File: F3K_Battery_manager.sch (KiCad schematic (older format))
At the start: 14 parts

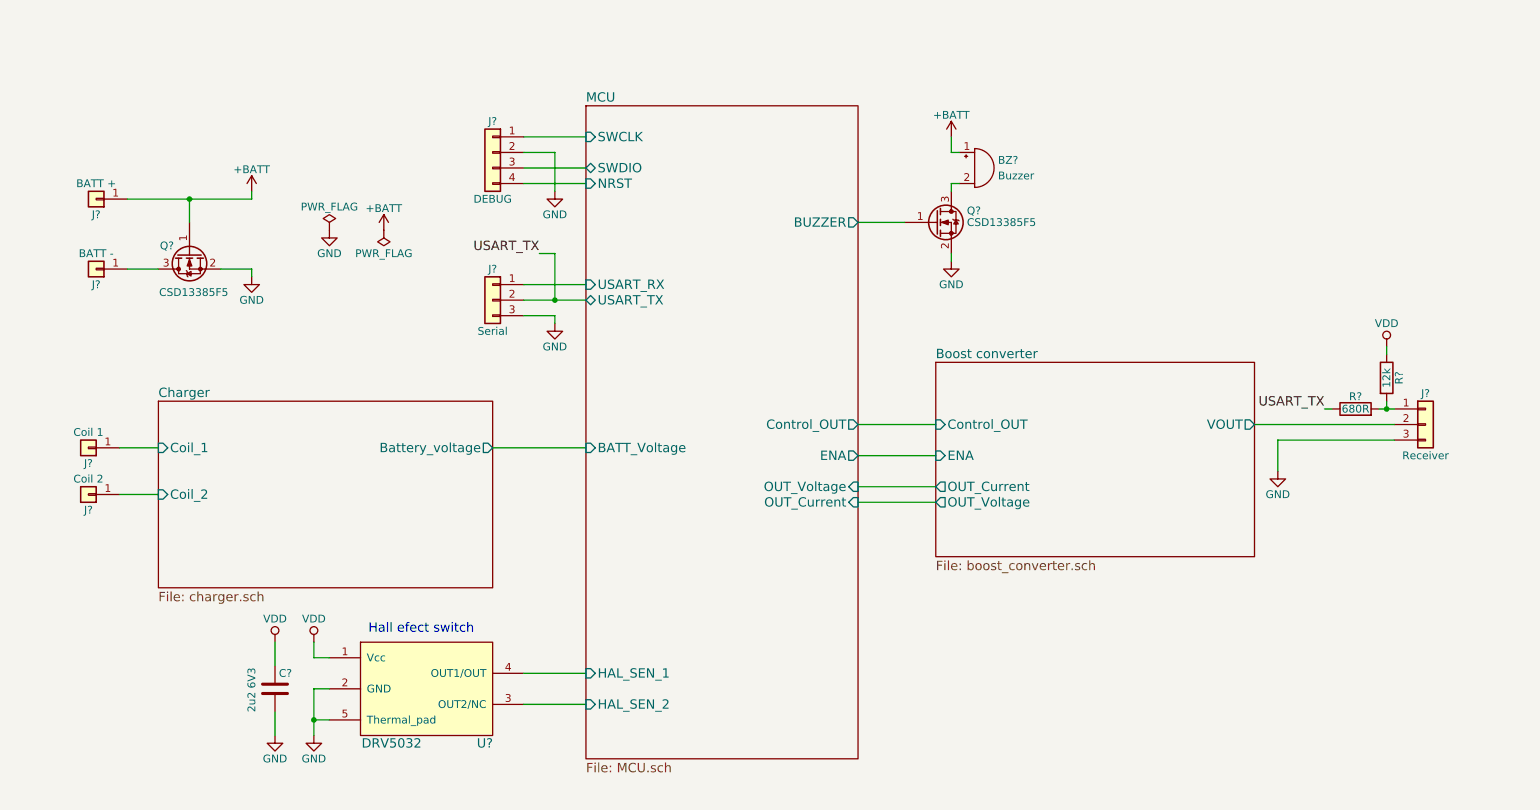
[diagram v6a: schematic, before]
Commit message: added few MPNs
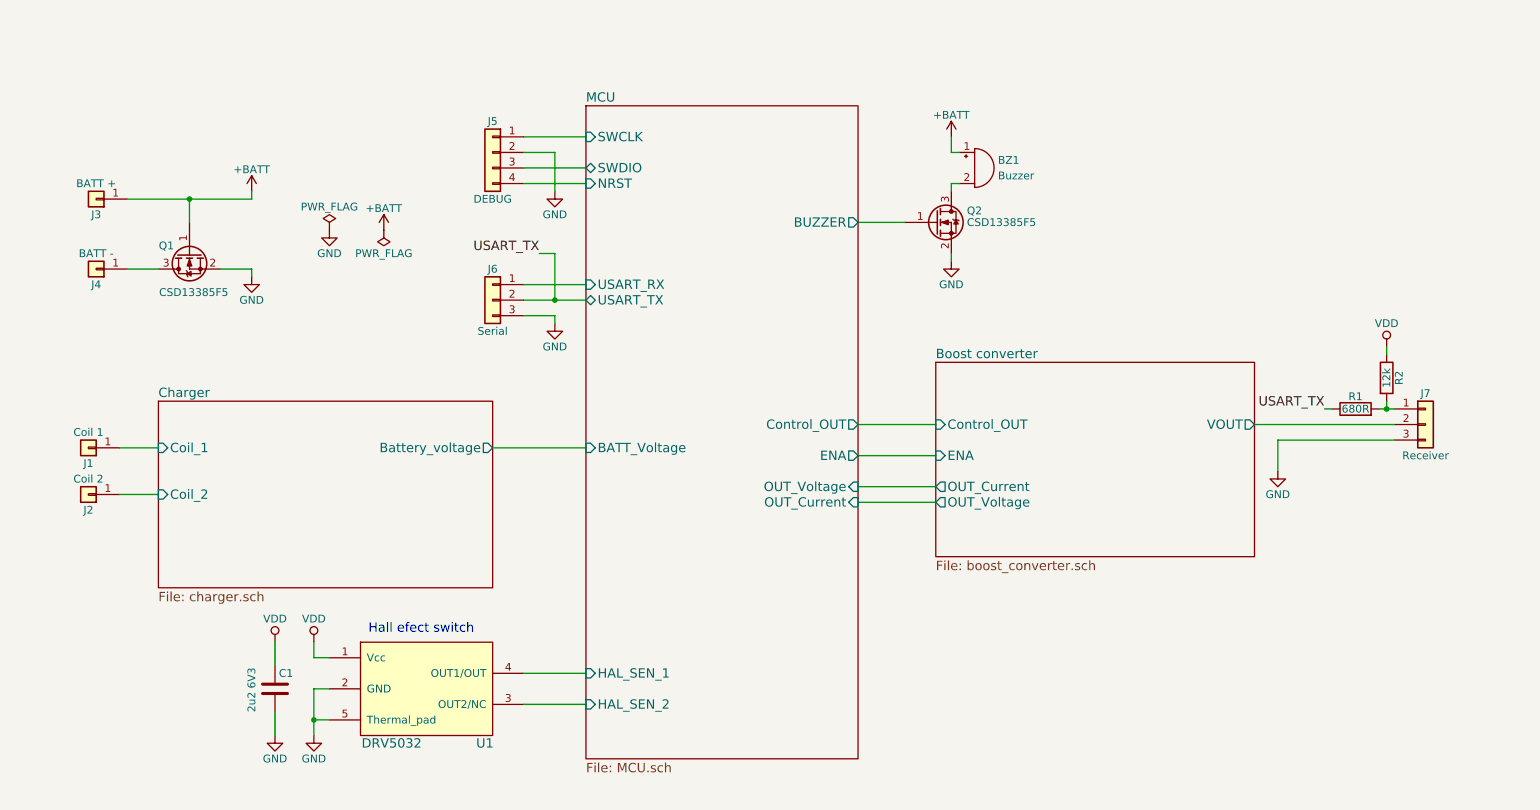
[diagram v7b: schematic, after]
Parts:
- C1: renamed from C?; footprint (none) -> Capacitors_SMD:C_0402; MPN (none) -> GRM155D80J225KE95D
- gave numbers to parts that had none: 13
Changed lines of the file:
@@
 $EndSheet
 $Comp
-L Conn_01x04 J?
+L Conn_01x04 J5
 U 1 1 5AA070CB
 P 4250 2250
-F 0 "J?" H 4250 2450 50  0000 C CNN
+F 0 "J5" H 4250 2450 50  0000 C CNN
 F 1 "DEBUG" H 4250 1950 50  0000 C CNN
 F 2 "" H 4250 2250 50  0001 C CNN
@@
 $EndComp
 $Comp
-L GND #PWR?
+L GND #PWR9
 U 1 1 5AA0735F
 P 4650 2500
-F 0 "#PWR?" H 4650 2250 50  0001 C CNN
+F 0 "#PWR9" H 4650 2250 50  0001 C CNN
 F 1 "GND" H 4650 2350 50  0000 C CNN
 F 2 "" H 4650 2500 50  0001 C CNN
@@
 $EndComp
 $Comp
-L GND #PWR?
+L GND #PWR10
 U 1 1 5AA07C91
 P 4650 3350
-F 0 "#PWR?" H 4650 3100 50  0001 C CNN
+F 0 "#PWR10" H 4650 3100 50  0001 C CNN
 F 1 "GND" H 4650 3200 50  0000 C CNN
 F 2 "" H 4650 3350 50  0001 C CNN
@@
 $EndComp
 $Comp
-L DRV5032 U?
+L DRV5032 U1
 U 1 1 5AA08B55
 P 3850 5700
-F 0 "U?" H 4200 5350 60  0000 C CNN
+F 0 "U1" H 4200 5350 60  0000 C CNN
 F 1 "DRV5032" H 3600 5350 60  0000 C CNN
 F 2 "lakotamm-sensor:X2SON_4_1.10x1.40mm" H 3900 5250 60  0001 C CNN
@@
 $EndComp
 $Comp
-L C C?
+L C C1
 U 1 1 5AA08E27
 P 2850 5700
-F 0 "C?" H 2875 5800 50  0000 L CNN
+F 0 "C1" H 2875 5800 50  0000 L CNN
 F 1 "2u2 6V3" V 2700 5550 50  0000 L CNN
-F 2 "" H 2888 5550 50  0001 C CNN
+F 2 "Capacitors_SMD:C_0402" H 2888 5550 50  0001 C CNN
 F 3 "" H 2850 5700 50  0001 C CNN
+F 4 "GRM155D80J225KE95D" H 2850 5700 60  0001 C CNN "MPN"
 	1    2850 5700
 	1    0    0    -1
@@
 	4850 3100 4450 3100
 Wire Wire Line
-	4450 3200 4650 3200
-Wire Wire Line
-	4650 3200 4850 3200
+	4450 3200 4850 3200
 Wire Wire Line
 	4450 3300 4650 3300
@@
 	4650 3300 4650 3350
 $Comp
-L GND #PWR?
+L GND #PWR6
 U 1 1 5AA09559
 P 3100 6000
-F 0 "#PWR?" H 3100 5750 50  0001 C CNN
+F 0 "#PWR6" H 3100 5750 50  0001 C CNN
 F 1 "GND" H 3100 5850 50  0000 C CNN
 F 2 "" H 3100 6000 50  0001 C CNN
@@
 	3200 5700 3100 5700
 Wire Wire Line
-	3100 5700 3100 5900
-Wire Wire Line
-	3100 5900 3100 6000
+	3100 5700 3100 6000
 Wire Wire Line
 	3200 5900 3100 5900
 Connection ~ 3100 5900
 $Comp
-L VDD #PWR?
+L VDD #PWR5
 U 1 1 5AA0982A
 P 3100 5400
-F 0 "#PWR?" H 3100 5250 50  0001 C CNN
+F 0 "#PWR5" H 3100 5250 50  0001 C CNN
 F 1 "VDD" H 3100 5550 50  0000 C CNN
 F 2 "" H 3100 5400 50  0001 C CNN
@@
 	3100 5500 3200 5500
 $Comp
-L VDD #PWR?
+L VDD #PWR3
 U 1 1 5AA09936
 P 2850 5400
-F 0 "#PWR?" H 2850 5250 50  0001 C CNN
+F 0 "#PWR3" H 2850 5250 50  0001 C CNN
 F 1 "VDD" H 2850 5550 50  0000 C CNN
 F 2 "" H 2850 5400 50  0001 C CNN
@@
 $EndComp
 $Comp
-L GND #PWR?
+L GND #PWR4
 U 1 1 5AA0996B
 P 2850 6000
-F 0 "#PWR?" H 2850 5750 50  0001 C CNN
+F 0 "#PWR4" H 2850 5750 50  0001 C CNN
 F 1 "GND" H 2850 5850 50  0000 C CNN
 F 2 "" H 2850 6000 50  0001 C CNN
@@
 	4450 5800 4850 5800
 $Comp
-L PWR_FLAG #FLG?
+L PWR_FLAG #FLG1
 U 1 1 5AA0B07D
 P 3200 2750
-F 0 "#FLG?" H 3200 2825 50  0001 C CNN
+F 0 "#FLG1" H 3200 2825 50  0001 C CNN
 F 1 "PWR_FLAG" H 3200 2900 50  0000 C CNN
 F 2 "" H 3200 2750 50  0001 C CNN
@@
 $EndComp
 $Comp
-L GND #PWR?
+L GND #PWR7
 U 1 1 5AA0B18B
 P 3200 2750
-F 0 "#PWR?" H 3200 2500 50  0001 C CNN
+F 0 "#PWR7" H 3200 2500 50  0001 C CNN
 F 1 "GND" H 3200 2600 50  0000 C CNN
 F 2 "" H 3200 2750 50  0001 C CNN
@@
 $EndComp
 $Comp
-L PWR_FLAG #FLG?
+L PWR_FLAG #FLG2
 U 1 1 5AA0B25E
 P 3550 2750
-F 0 "#FLG?" H 3550 2825 50  0001 C CNN
+F 0 "#FLG2" H 3550 2825 50  0001 C CNN
 F 1 "PWR_FLAG" H 3550 2900 50  0000 C CNN
 F 2 "" H 3550 2750 50  0001 C CNN
@@
 $EndComp
 $Comp
-L +BATT #PWR?
+L +BATT #PWR8
 U 1 1 5AA0B29D
 P 3550 2750
-F 0 "#PWR?" H 3550 2600 50  0001 C CNN
+F 0 "#PWR8" H 3550 2600 50  0001 C CNN
 F 1 "+BATT" H 3550 2890 50  0000 C CNN
 F 2 "" H 3550 2750 50  0001 C CNN
@@
 $EndComp
 $Comp
-L Buzzer BZ?
+L Buzzer BZ1
 U 1 1 5AA0FFE4
 P 7350 2350
-F 0 "BZ?" H 7500 2400 50  0000 L CNN
+F 0 "BZ1" H 7500 2400 50  0000 L CNN
 F 1 "Buzzer" H 7500 2300 50  0000 L CNN
 F 2 "" V 7325 2450 50  0001 C CNN
@@
 	7200 2450 7200 2500
 $Comp
-L GND #PWR?
+L GND #PWR12
 U 1 1 5AA112B0
 P 7200 2950
-F 0 "#PWR?" H 7200 2700 50  0001 C CNN
+F 0 "#PWR12" H 7200 2700 50  0001 C CNN
 F 1 "GND" H 7200 2800 50  0000 C CNN
 F 2 "" H 7200 2950 50  0001 C CNN
@@
 $EndSheet
 $Comp
-L +BATT #PWR?
+L +BATT #PWR11
 U 1 1 5AA3F1DA
 P 7200 2150
-F 0 "#PWR?" H 7200 2000 50  0001 C CNN
+F 0 "#PWR11" H 7200 2000 50  0001 C CNN
 F 1 "+BATT" H 7200 2290 50  0000 C CNN
 F 2 "" H 7200 2150 50  0001 C CNN
@@
 	6600 4000 7100 4000
 $Comp
-L Conn_01x03 J?
+L Conn_01x03 J7
 U 1 1 5AA45C5D
 P 10250 4000
-F 0 "J?" H 10250 4200 50  0000 C CNN
+F 0 "J7" H 10250 4200 50  0000 C CNN
 F 1 "Receiver" H 10250 3800 50  0000 C CNN
 F 2 "" H 10250 4000 50  0001 C CNN
@@
 	9150 4000 10050 4000
 $Comp
-L GND #PWR?
+L GND #PWR13
 U 1 1 5AA460B2
 P 9300 4300
-F 0 "#PWR?" H 9300 4050 50  0001 C CNN
+F 0 "#PWR13" H 9300 4050 50  0001 C CNN
 F 1 "GND" H 9300 4150 50  0000 C CNN
 F 2 "" H 9300 4300 50  0001 C CNN
@@
 	9300 4100 9300 4300
 $Comp
-L Conn_01x03 J?
+L Conn_01x03 J6
 U 1 1 5AA46769
 P 4250 3200
-F 0 "J?" H 4250 3400 50  0000 C CNN
+F 0 "J6" H 4250 3400 50  0000 C CNN
 F 1 "Serial" H 4250 3000 50  0000 C CNN
 F 2 "" H 4250 3200 50  0001 C CNN
@@
 Hall efect switch\n
 $Comp
-L R R?
+L R R1
 U 1 1 5AA59CAF
 P 9800 3900
-F 0 "R?" V 9880 3900 50  0000 C CNN
+F 0 "R1" V 9880 3900 50  0000 C CNN
 F 1 "680R" V 9800 3900 50  0000 C CNN
 F 2 "" V 9730 3900 50  0001 C CNN
@@
 $EndComp
 Wire Wire Line
-	9950 3900 10000 3900
-Wire Wire Line
-	10000 3900 10050 3900
+	9950 3900 10050 3900
 Text Label 4550 2900 2    60   ~ 0
 USART_TX
@@
 	9600 3900 9650 3900
 $Comp
-L R R?
+L R R2
 U 1 1 5AA65085
 P 10000 3700
-F 0 "R?" V 10080 3700 50  0000 C CNN
+F 0 "R2" V 10080 3700 50  0000 C CNN
 F 1 "12k" V 10000 3700 50  0000 C CNN
 F 2 "" V 9930 3700 50  0001 C CNN
@@
 Connection ~ 10000 3900
 $Comp
-L VDD #PWR?
+L VDD #PWR14
 U 1 1 5AA65702
 P 10000 3500
-F 0 "#PWR?" H 10000 3350 50  0001 C CNN
+F 0 "#PWR14" H 10000 3350 50  0001 C CNN
 F 1 "VDD" H 10000 3650 50  0000 C CNN
 F 2 "" H 10000 3500 50  0001 C CNN
@@
 	4250 4150 4850 4150
 $Comp
-L CSD13385F5 Q?
+L CSD13385F5 Q2
 U 1 1 5AA727C4
 P 7100 2700
-F 0 "Q?" H 7300 2775 50  0000 L CNN
+F 0 "Q2" H 7300 2775 50  0000 L CNN
 F 1 "CSD13385F5" H 7300 2700 50  0000 L CNN
 F 2 "" H 7300 2625 50  0001 L CIN
@@
 $EndComp
 $Comp
-L CSD13385F5 Q?
+L CSD13385F5 Q1
 U 1 1 5AA728A9
 P 2300 2900
-F 0 "Q?" V 2250 3000 50  0000 L CNN
+F 0 "Q1" V 2250 3000 50  0000 L CNN
 F 1 "CSD13385F5" V 2550 2650 50  0000 L CNN
 F 2 "" H 2500 2825 50  0001 L CIN
@@
 $EndComp
 $Comp
-L Conn_01x01 J?
+L Conn_01x01 J3
 U 1 1 5AA73103
 P 1700 2550
-F 0 "J?" H 1700 2650 50  0000 C CNN
+F 0 "J3" H 1700 2650 50  0000 C CNN
 F 1 "BATT +" H 1700 2450 50  0000 C CNN
 F 2 "" H 1700 2550 50  0001 C CNN
@@
 $EndComp
 $Comp
-L Conn_01x01 J?
+L Conn_01x01 J4
 U 1 1 5AA7332B
 P 1700 3000
-F 0 "J?" H 1700 3100 50  0000 C CNN
+F 0 "J4" H 1700 3100 50  0000 C CNN
 F 1 "BATT -" H 1700 2900 50  0000 C CNN
 F 2 "" H 1700 3000 50  0001 C CNN
@@
 	1900 3000 2100 3000
 Wire Wire Line
-	1900 2550 2300 2550
-Wire Wire Line
-	2300 2550 2700 2550
+	1900 2550 2700 2550
 Wire Wire Line
 	2300 2550 2300 2700
 $Comp
-L +BATT #PWR?
+L +BATT #PWR1
 U 1 1 5AA74E47
 P 2700 2500
-F 0 "#PWR?" H 2700 2350 50  0001 C CNN
+F 0 "#PWR1" H 2700 2350 50  0001 C CNN
 F 1 "+BATT" H 2700 2640 50  0000 C CNN
 F 2 "" H 2700 2500 50  0001 C CNN
@@
 Connection ~ 2300 2550
 $Comp
-L GND #PWR?
+L GND #PWR2
 U 1 1 5AA7526D
 P 2700 3050
-F 0 "#PWR?" H 2700 2800 50  0001 C CNN
+F 0 "#PWR2" H 2700 2800 50  0001 C CNN
 F 1 "GND" H 2700 2900 50  0000 C CNN
 F 2 "" H 2700 3050 50  0001 C CNN
@@
 	2700 3000 2700 3050
 $Comp
-L Conn_01x01 J?
+L Conn_01x01 J1
 U 1 1 5AA76BD4
 P 1650 4150
-F 0 "J?" H 1650 4250 50  0000 C CNN
+F 0 "J1" H 1650 4250 50  0000 C CNN
 F 1 "Coil 1" H 1650 4050 50  0000 C CNN
 F 2 "" H 1650 4150 50  0001 C CNN
@@
 $EndComp
 $Comp
-L Conn_01x01 J?
+L Conn_01x01 J2
 U 1 1 5AA76CB0
 P 1650 4450
-F 0 "J?" H 1650 4550 50  0000 C CNN
+F 0 "J2" H 1650 4550 50  0000 C CNN
 F 1 "Coil 2" H 1650 4350 50  0000 C CNN
 F 2 "" H 1650 4450 50  0001 C CNN

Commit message: Progress on the charging circuit
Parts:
- removed J1: Coil 1, symbol Conn_01x01
- removed J2: Coil 2, symbol Conn_01x01
- removed J3: BATT +, symbol Conn_01x01
- removed J4: BATT -, symbol Conn_01x01
- added J?: Battery, symbol Conn_01x04
- added J?: Coil, symbol Conn_01x02
- J5: value DEBUG -> Debug
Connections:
- net +BATT: now also J?.3 (Pin_3)
- net Charger/Coil_1: now also J?.2 (Pin_2)
- net Charger/Coil_2: now also J?.1 (Pin_1)
- net at Q1.3 (D): now also J?.4 (Pin_4)
- new net Thermistor: J?.2 (Pin_2)
- new net Thermistor_OFF: J?.1 (Pin_1)
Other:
- moved on the sheet: Q1
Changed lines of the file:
@@
 F7 "HAL_SEN_2" I L 4850 5800 60
 F8 "BUZZER" O R 6600 2700 60
-F9 "Control_OUT" O R 6600 4000 60
-F10 "ENA" O R 6600 4200 60
-F11 "OUT_Voltage" I R 6600 4400 60
-F12 "OUT_Current" I R 6600 4500 60
-F13 "BATT_Voltage" I L 4850 4150 60
-F14 "USART_TX" B L 4850 3200 60
+F9 "OUT_Voltage" I R 6600 4400 60
+F10 "OUT_Current" I R 6600 4500 60
+F11 "BATT_Voltage" I L 4850 4150 60
+F12 "USART_TX" B L 4850 3200 60
+F13 "~CHARGING" I L 4850 4350 60
+F14 "Voltage_control" O R 6600 4000 60
+F15 "Enable_boost" O R 6600 4200 60
 $EndSheet
 $Comp
@@
 P 4250 2250
 F 0 "J5" H 4250 2450 50  0000 C CNN
-F 1 "DEBUG" H 4250 1950 50  0000 C CNN
+F 1 "Debug" H 4250 1950 50  0000 C CNN
 F 2 "" H 4250 2250 50  0001 C CNN
 F 3 "" H 4250 2250 50  0001 C CNN
@@
 Wire Wire Line
 	6600 2700 6900 2700
-$Sheet
-S 2100 3850 2150 1200
-U 5AA3AC9F
-F0 "Charger" 60
-F1 "charger.sch" 60
-F2 "Coil_1" I L 2100 4150 60
-F3 "Coil_2" I L 2100 4450 60
-F4 "Battery_voltage" O R 4250 4150 60
-$EndSheet
 $Comp
 L +BATT #PWR11
@@
 F1 "boost_converter.sch" 60
 F2 "VOUT" O R 9150 4000 60
-F3 "Control_OUT" I L 7100 4000 60
-F4 "ENA" I L 7100 4200 60
-F5 "OUT_Current" O L 7100 4400 60
-F6 "OUT_Voltage" O L 7100 4500 60
+F3 "ENA" I L 7100 4200 60
+F4 "OUT_Current" O L 7100 4400 60
+F5 "OUT_Voltage" O L 7100 4500 60
+F6 "Voltage_control" I L 7100 4000 60
 $EndSheet
 Wire Wire Line
@@
 	10000 3500 10000 3550
 Wire Wire Line
-	1850 4150 2100 4150
-Wire Wire Line
 	4250 4150 4850 4150
 $Comp
@@
 L CSD13385F5 Q1
 U 1 1 5AA728A9
-P 2300 2900
-F 0 "Q1" V 2250 3000 50  0000 L CNN
-F 1 "CSD13385F5" V 2550 2650 50  0000 L CNN
-F 2 "" H 2500 2825 50  0001 L CIN
-F 3 "http://www.ti.com/lit/ds/symlink/csd13385f5.pdf" H 1600 2600 50  0001 L CNN
-F 4 "CSD13385F5" H 2400 3200 60  0001 C CNN "MPN"
-	1    2300 2900
+P 2300 2800
+F 0 "Q1" V 2250 2900 50  0000 L CNN
+F 1 "CSD13385F5" V 2550 2550 50  0000 L CNN
+F 2 "" H 2500 2725 50  0001 L CIN
+F 3 "http://www.ti.com/lit/ds/symlink/csd13385f5.pdf" H 1600 2500 50  0001 L CNN
+F 4 "CSD13385F5" H 2400 3100 60  0001 C CNN "MPN"
+	1    2300 2800
 	0    -1   1    0
 $EndComp
-$Comp
-L Conn_01x01 J3
-U 1 1 5AA73103
-P 1700 2550
-F 0 "J3" H 1700 2650 50  0000 C CNN
-F 1 "BATT +" H 1700 2450 50  0000 C CNN
-F 2 "" H 1700 2550 50  0001 C CNN
-F 3 "" H 1700 2550 50  0001 C CNN
-	1    1700 2550
-	-1   0    0    1
-$EndComp
-$Comp
-L Conn_01x01 J4
-U 1 1 5AA7332B
-P 1700 3000
-F 0 "J4" H 1700 3100 50  0000 C CNN
-F 1 "BATT -" H 1700 2900 50  0000 C CNN
-F 2 "" H 1700 3000 50  0001 C CNN
-F 3 "" H 1700 3000 50  0001 C CNN
-	1    1700 3000
-	-1   0    0    1
-$EndComp
-Wire Wire Line
-	1900 3000 2100 3000
-Wire Wire Line
-	1900 2550 2700 2550
-Wire Wire Line
-	2300 2550 2300 2700
+Wire Wire Line
+	1900 2550 2800 2550
+Wire Wire Line
+	2300 2550 2300 2550
 $Comp
 L +BATT #PWR1
 U 1 1 5AA74E47
-P 2700 2500
-F 0 "#PWR1" H 2700 2350 50  0001 C CNN
-F 1 "+BATT" H 2700 2640 50  0000 C CNN
-F 2 "" H 2700 2500 50  0001 C CNN
-F 3 "" H 2700 2500 50  0001 C CNN
-	1    2700 2500
-	1    0    0    -1
-$EndComp
-Wire Wire Line
-	2700 2550 2700 2500
+P 2800 2500
+F 0 "#PWR1" H 2800 2350 50  0001 C CNN
+F 1 "+BATT" H 2800 2640 50  0000 C CNN
+F 2 "" H 2800 2500 50  0001 C CNN
+F 3 "" H 2800 2500 50  0001 C CNN
+	1    2800 2500
+	1    0    0    -1
+$EndComp
+Wire Wire Line
+	2800 2550 2800 2500
 Connection ~ 2300 2550
 $Comp
 L GND #PWR2
 U 1 1 5AA7526D
-P 2700 3050
-F 0 "#PWR2" H 2700 2800 50  0001 C CNN
-F 1 "GND" H 2700 2900 50  0000 C CNN
-F 2 "" H 2700 3050 50  0001 C CNN
-F 3 "" H 2700 3050 50  0001 C CNN
-	1    2700 3050
-	1    0    0    -1
-$EndComp
-Wire Wire Line
-	2500 3000 2700 3000
-Wire Wire Line
-	2700 3000 2700 3050
-$Comp
-L Conn_01x01 J1
-U 1 1 5AA76BD4
-P 1650 4150
-F 0 "J1" H 1650 4250 50  0000 C CNN
-F 1 "Coil 1" H 1650 4050 50  0000 C CNN
-F 2 "" H 1650 4150 50  0001 C CNN
-F 3 "" H 1650 4150 50  0001 C CNN
-	1    1650 4150
+P 2700 2950
+F 0 "#PWR2" H 2700 2700 50  0001 C CNN
+F 1 "GND" H 2700 2800 50  0000 C CNN
+F 2 "" H 2700 2950 50  0001 C CNN
+F 3 "" H 2700 2950 50  0001 C CNN
+	1    2700 2950
+	1    0    0    -1
+$EndComp
+Wire Wire Line
+	2500 2900 2700 2900
+Wire Wire Line
+	2700 2900 2700 2950
+$Comp
+L Conn_01x04 J?
+U 1 1 5AB08D80
+P 1700 2450
+F 0 "J?" H 1700 2650 50  0000 C CNN
+F 1 "Battery" H 1700 2150 50  0000 C CNN
+F 2 "" H 1700 2450 50  0001 C CNN
+F 3 "" H 1700 2450 50  0001 C CNN
+	1    1700 2450
+	-1   0    0    -1
+$EndComp
+Wire Wire Line
+	1900 2650 2000 2650
+Wire Wire Line
+	2000 2650 2000 2900
+Wire Wire Line
+	2000 2900 2100 2900
+Text Label 2000 2450 0    60   ~ 0
+Thermistor
+Wire Wire Line
+	1900 2450 2000 2450
+Wire Wire Line
+	2300 2550 2300 2600
+$Sheet
+S 2100 3850 2150 1200
+U 5AA3AC9F
+F0 "Charger" 60
+F1 "charger.sch" 60
+F2 "Coil_1" I L 2100 4050 60
+F3 "Coil_2" I L 2100 4150 60
+F4 "Battery_voltage" O R 4250 4150 60
+F5 "Thermistor" I L 2100 4450 60
+F6 "~CHARGING" O R 4250 4350 60
+F7 "Charge_control" I R 4250 4550 60
+F8 "Thermistor_OFF" I L 2100 4600 60
+$EndSheet
+$Comp
+L Conn_01x02 J?
+U 1 1 5AB11894
+P 1700 4150
+F 0 "J?" H 1700 4250 50  0000 C CNN
+F 1 "Coil" H 1700 3950 50  0000 C CNN
+F 2 "" H 1700 4150 50  0001 C CNN
+F 3 "" H 1700 4150 50  0001 C CNN
+	1    1700 4150
 	-1   0    0    1
 $EndComp
-$Comp
-L Conn_01x01 J2
-U 1 1 5AA76CB0
-P 1650 4450
-F 0 "J2" H 1650 4550 50  0000 C CNN
-F 1 "Coil 2" H 1650 4350 50  0000 C CNN
-F 2 "" H 1650 4450 50  0001 C CNN
-F 3 "" H 1650 4450 50  0001 C CNN
-	1    1650 4450
-	-1   0    0    1
-$EndComp
-Wire Wire Line
-	1850 4450 2100 4450
+Wire Wire Line
+	2100 4050 1900 4050
+Wire Wire Line
+	1900 4150 2100 4150
+Text Label 2000 4450 2    60   ~ 0
+Thermistor
+Wire Wire Line
+	2000 4450 2100 4450
+Wire Wire Line
+	4250 4350 4850 4350
+Text Label 2000 2350 0    60   ~ 0
+Thermistor_OFF
+Wire Wire Line
+	1900 2350 2000 2350
+Text Label 2000 4600 2    60   ~ 0
+Thermistor_OFF
+Wire Wire Line
+	2000 4600 2100 4600
 $EndSCHEMATC
